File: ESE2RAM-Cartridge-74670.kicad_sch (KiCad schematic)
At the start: 27 parts, among them CN1 BUS_MSX, IC1 4M SRAM, IC2 4M SRAM, J1 8M, U1 74HC670, U2 74HC670, U3 74AHC138, U4 74AHC00, U5 74AHC32

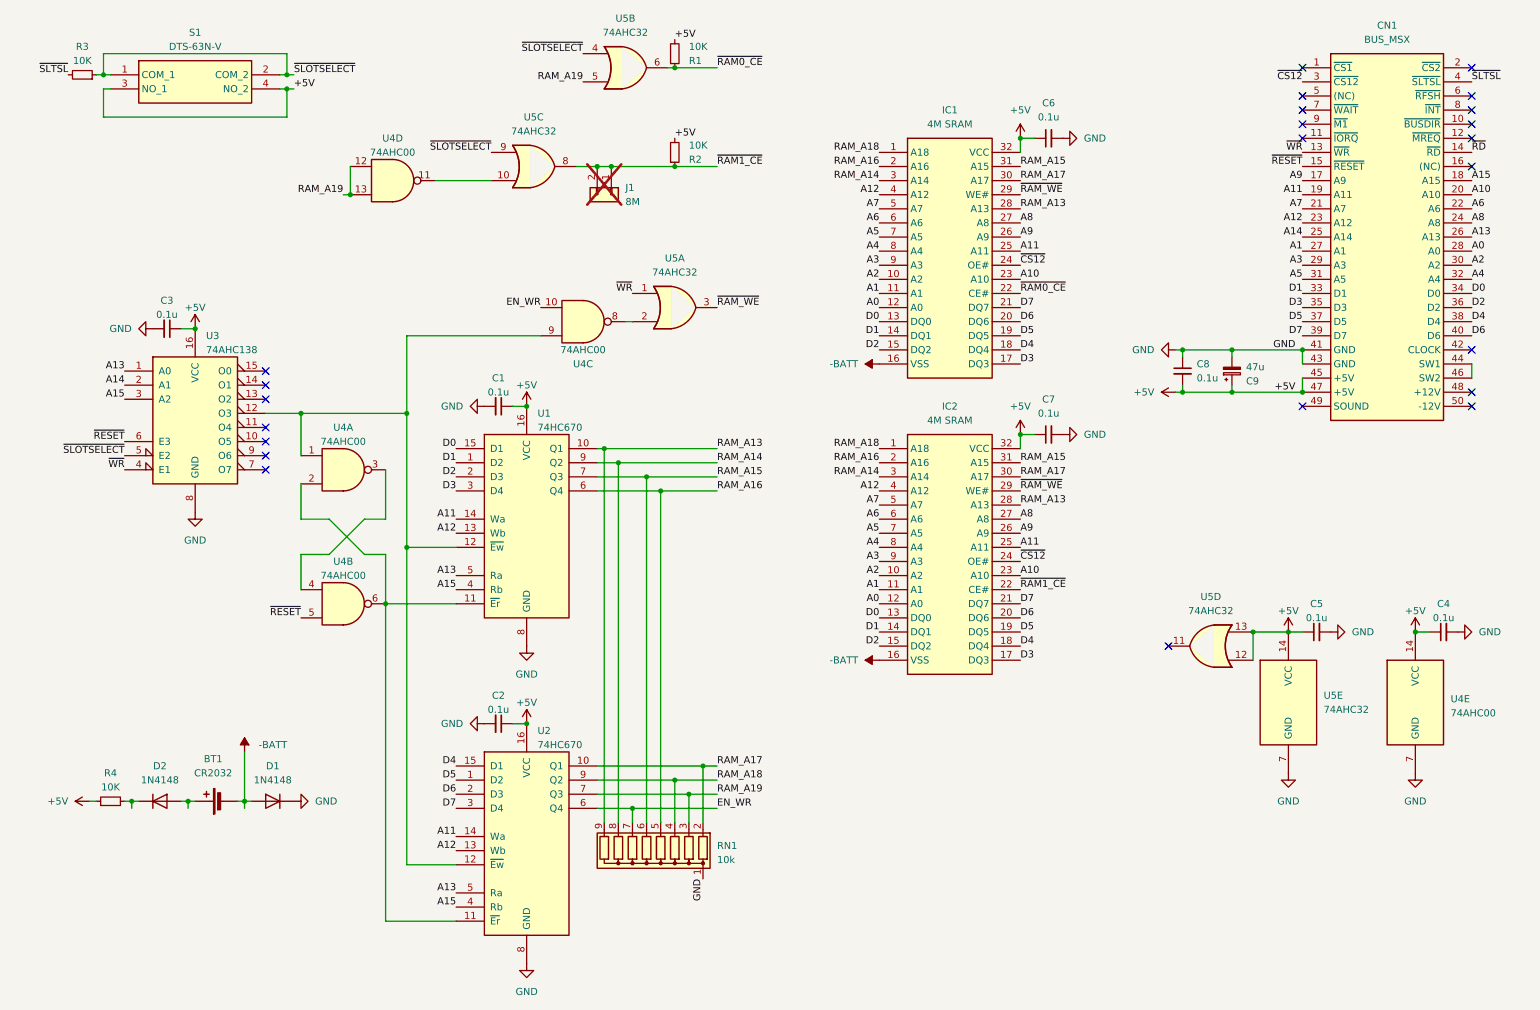
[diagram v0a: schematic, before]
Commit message: Modified ESE2BOOT.COM & Schematic
ESE2BOOT.COMのバグ修正
Fixed a bug in ESE2BOOT.COM
回路図データの微修正
Minor corrections to schematic data.
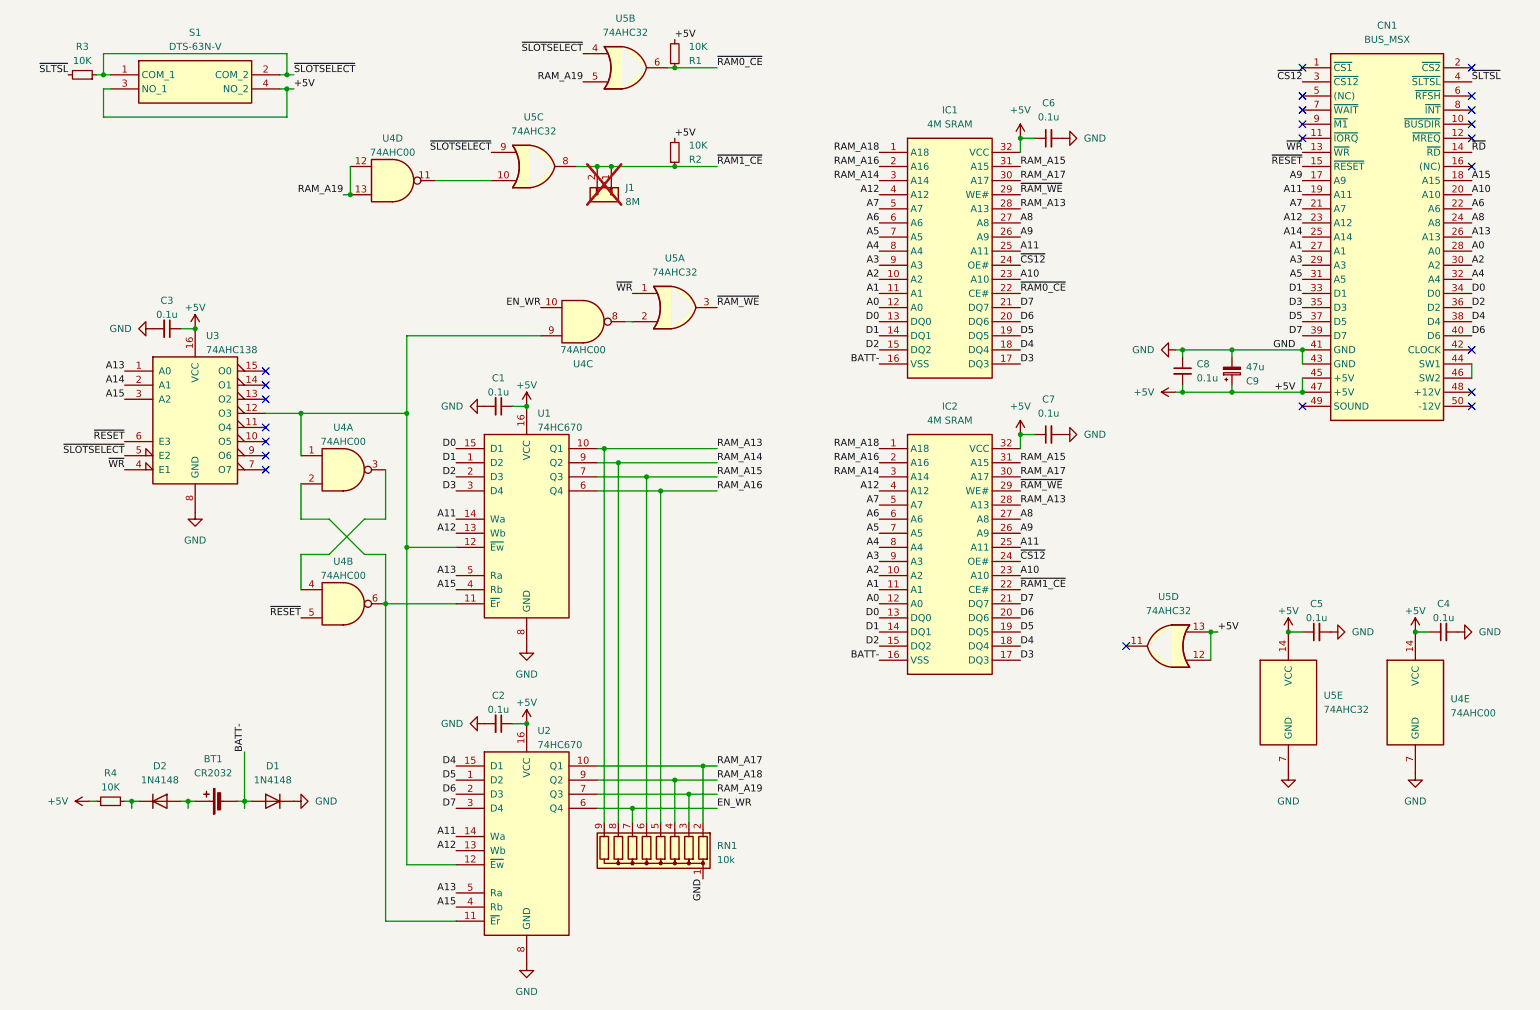
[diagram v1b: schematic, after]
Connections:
- net -BATT renamed BATT-
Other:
- moved on the sheet: U5D
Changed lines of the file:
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@@
   (title_block
     (title "ESE2RAM Cartridge (74x670 version)")
-    (date "2025-04-06")
+    (date "2025-04-11")
     (rev "6")
     (company "Goripon Hardware")
@@
   (junction (at 60.96 31.75) (diameter 0) (color 0 0 0 0)
   )
+  (junction (at 227.33 129.54) (diameter 0) (color 0 0 0 0)
+  )
   (junction (at 130.81 45.72) (diameter 0) (color 0 0 0 0)
   )
@@
   )
   (junction (at 63.5 90.17) (diameter 0) (color 0 0 0 0)
-  )
-  (junction (at 234.95 129.54) (diameter 0) (color 0 0 0 0)
   )
   (junction (at 130.81 156.21) (diameter 0) (color 0 0 0 0)
@@
   (no_connect (at 274.32 88.9))
   (no_connect (at 243.84 33.02))
-  (no_connect (at 219.71 132.08))
+  (no_connect (at 212.09 132.08))
   (no_connect (at 57.15 85.09))
-  (wire (pts (xy 234.95 129.54) (xy 241.3 129.54))
-    (stroke (width 0) (type default))
-  )
   (wire (pts (xy 135.89 153.67) (xy 135.89 163.83))
     (stroke (width 0) (type default))
@@
     (stroke (width 0) (type default))
   )
+  (wire (pts (xy 227.33 129.54) (xy 228.6 129.54))
+    (stroke (width 0) (type default))
+  )
   (wire (pts (xy 116.84 156.21) (xy 130.81 156.21))
     (stroke (width 0) (type default))
@@
     (stroke (width 0) (type default))
   )
-  (wire (pts (xy 234.95 134.62) (xy 234.95 129.54))
+  (wire (pts (xy 227.33 134.62) (xy 227.33 129.54))
     (stroke (width 0) (type default))
   )
@@
     (effects (font (size 1.27 1.27)) (justify left bottom))
   )
+  (label "BATT-" (at 167.64 81.28 180) (fields_autoplaced)
+    (effects (font (size 1.27 1.27)) (justify right bottom))
+  )
   (label "RAM_A16" (at 138.43 104.14 0) (fields_autoplaced)
     (effects (font (size 1.27 1.27)) (justify left bottom))
@@
     (effects (font (size 1.27 1.27)) (justify left bottom))
   )
+  (label "BATT-" (at 53.34 151.13 90) (fields_autoplaced)
+    (effects (font (size 1.27 1.27)) (justify left bottom))
+  )
   (label "RAM_A19" (at 71.12 50.8 180) (fields_autoplaced)
     (effects (font (size 1.27 1.27)) (justify right bottom))
@@
     (effects (font (size 1.27 1.27)) (justify right bottom))
   )
+  (label "+5V" (at 228.6 129.54 0) (fields_autoplaced)
+    (effects (font (size 1.27 1.27)) (justify left bottom))
+  )
   (label "D0" (at 167.64 127 180) (fields_autoplaced)
     (effects (font (size 1.27 1.27)) (justify right bottom))
@@
   (label "A2" (at 274.32 63.5 0) (fields_autoplaced)
     (effects (font (size 1.27 1.27)) (justify left bottom))
+  )
+  (label "BATT-" (at 167.64 134.62 180) (fields_autoplaced)
+    (effects (font (size 1.27 1.27)) (justify right bottom))
   )
   (label "D3" (at 243.84 71.12 180) (fields_autoplaced)
@@
       (effects (font (size 1.27 1.27)) hide)
     )
-    (property "Datasheet" "https://www.ti.com/lit/ds/symlink/sn74ahc32.pdf" (at 241.3 142.24 0)
+    (property "Datasheet" "http://www.ti.com/lit/gpn/sn74HC32" (at 241.3 142.24 0)
       (effects (font (size 1.27 1.27)) hide)
     )
@@
       (effects (font (size 1.27 1.27)) hide)
     )
-    (property "Datasheet" "https://www.ti.com/lit/ds/symlink/sn74ahc32.pdf" (at 121.92 27.94 0)
+    (property "Datasheet" "http://www.ti.com/lit/gpn/sn74HC32" (at 121.92 27.94 0)
       (effects (font (size 1.27 1.27)) hide)
     )
@@
         (path "/63ac4003-bef6-4a96-a792-1e8f39f552e9"
           (reference "#PWR019") (unit 1)
-        )
-      )
-    )
-  )
-  (symbol (lib_id "power:-BATT") (at 167.64 134.62 90) (unit 1)
-    (in_bom yes) (on_board yes) (dnp no) (fields_autoplaced)
-    (property "Reference" "#PWR021" (at 171.45 134.62 0)
-      (effects (font (size 1.27 1.27)) hide)
-    )
-    (property "Value" "-BATT" (at 163.83 134.62 90)
-      (effects (font (size 1.27 1.27)) (justify left))
-    )
-    (property "Footprint" "" (at 167.64 134.62 0)
-      (effects (font (size 1.27 1.27)) hide)
-    )
-    (property "Datasheet" "" (at 167.64 134.62 0)
-      (effects (font (size 1.27 1.27)) hide)
-    )
-    (pin "1")
-    (instances
-      (project "ESE2RAM-Cartridge-74670"
-        (path "/63ac4003-bef6-4a96-a792-1e8f39f552e9"
-          (reference "#PWR021") (unit 1)
         )
       )
@@
     )
   )
-  (symbol (lib_id "_GoriponsoftLibrary:74HC32") (at 227.33 132.08 180) (unit 4)
-    (in_bom yes) (on_board yes) (dnp no) (fields_autoplaced)
-    (property "Reference" "U5" (at 227.33 123.19 0)
-      (effects (font (size 1.27 1.27)))
-    )
-    (property "Value" "74AHC32" (at 227.33 125.73 0)
-      (effects (font (size 1.27 1.27)))
-    )
-    (property "Footprint" "ProjectLibrary:DIP14_300mil_FineLongPad" (at 227.33 132.08 0)
-      (effects (font (size 1.27 1.27)) hide)
-    )
-    (property "Datasheet" "https://www.ti.com/lit/ds/symlink/sn74ahc32.pdf" (at 227.33 132.08 0)
+  (symbol (lib_id "_GoriponsoftLibrary:74HC32") (at 219.71 132.08 180) (unit 4)
+    (in_bom yes) (on_board yes) (dnp no) (fields_autoplaced)
+    (property "Reference" "U5" (at 219.71 123.19 0)
+      (effects (font (size 1.27 1.27)))
+    )
+    (property "Value" "74AHC32" (at 219.71 125.73 0)
+      (effects (font (size 1.27 1.27)))
+    )
+    (property "Footprint" "ProjectLibrary:DIP14_300mil_FineLongPad" (at 219.71 132.08 0)
+      (effects (font (size 1.27 1.27)) hide)
+    )
+    (property "Datasheet" "http://www.ti.com/lit/gpn/sn74HC32" (at 219.71 132.08 0)
       (effects (font (size 1.27 1.27)) hide)
     )
@@
     )
   )
-  (symbol (lib_id "power:-BATT") (at 53.34 151.13 0) (unit 1)
-    (in_bom yes) (on_board yes) (dnp no) (fields_autoplaced)
-    (property "Reference" "#PWR014" (at 53.34 154.94 0)
-      (effects (font (size 1.27 1.27)) hide)
-    )
-    (property "Value" "-BATT" (at 55.88 149.86 0)
-      (effects (font (size 1.27 1.27)) (justify left))
-    )
-    (property "Footprint" "" (at 53.34 151.13 0)
-      (effects (font (size 1.27 1.27)) hide)
-    )
-    (property "Datasheet" "" (at 53.34 151.13 0)
-      (effects (font (size 1.27 1.27)) hide)
-    )
-    (pin "1")
-    (instances
-      (project "ESE2RAM-Cartridge-74670"
-        (path "/63ac4003-bef6-4a96-a792-1e8f39f552e9"
-          (reference "#PWR014") (unit 1)
-        )
-      )
-    )
-  )
   (symbol (lib_id "Device:C_Small") (at 39.37 74.93 270) (mirror x) (unit 1)
     (in_bom yes) (on_board yes) (dnp no)
@@
     )
   )
-  (symbol (lib_id "power:-BATT") (at 167.64 81.28 90) (unit 1)
-    (in_bom yes) (on_board yes) (dnp no) (fields_autoplaced)
-    (property "Reference" "#PWR015" (at 171.45 81.28 0)
-      (effects (font (size 1.27 1.27)) hide)
-    )
-    (property "Value" "-BATT" (at 163.83 81.28 90)
-      (effects (font (size 1.27 1.27)) (justify left))
-    )
-    (property "Footprint" "" (at 167.64 81.28 0)
-      (effects (font (size 1.27 1.27)) hide)
-    )
-    (property "Datasheet" "" (at 167.64 81.28 0)
-      (effects (font (size 1.27 1.27)) hide)
-    )
-    (pin "1")
-    (instances
-      (project "ESE2RAM-Cartridge-74670"
-        (path "/63ac4003-bef6-4a96-a792-1e8f39f552e9"
-          (reference "#PWR015") (unit 1)
-        )
-      )
-    )
-  )
   (symbol (lib_id "Device:C_Small") (at 222.25 82.55 0) (unit 1)
     (in_bom yes) (on_board yes) (dnp no)
@@
   )
   (symbol (lib_id "power:+5V") (at 220.98 86.36 90) (unit 1)
-    (in_bom yes) (on_board yes) (dnp no) (fields_autoplaced)
+    (in_bom yes) (on_board yes) (dnp no)
     (property "Reference" "#PWR06" (at 224.79 86.36 0)
       (effects (font (size 1.27 1.27)) hide)
@@
       (effects (font (size 1.27 1.27)) hide)
     )
-    (property "Datasheet" "https://www.ti.com/lit/ds/symlink/sn74ahc32.pdf" (at 105.41 45.72 0)
+    (property "Datasheet" "http://www.ti.com/lit/gpn/sn74HC32" (at 105.41 45.72 0)
       (effects (font (size 1.27 1.27)) hide)
     )
@@
       (effects (font (size 1.27 1.27)) hide)
     )
-    (property "Datasheet" "https://www.ti.com/lit/ds/symlink/sn74ahc32.pdf" (at 130.81 71.12 0)
-      (effects (font (size 1.27 1.27)) hide)
-    )
+    (property "Datasheet" "http://www.ti.com/lit/gpn/sn74HC32" (at 130.81 71.12 0)
+      (effects (font (size 1.27 1.27)) hide)
+    )
